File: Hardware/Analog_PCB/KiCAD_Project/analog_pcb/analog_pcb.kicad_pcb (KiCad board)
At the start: 4 copper layers, 44.4 x 31.8 mm, 36 parts, among them J1 Board to Board, U1 555, U2 LF356, U3 LTC1569-6

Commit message: Analog PCB Rev 1.0 complete.
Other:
- board text added: "+5"
- board text added: "-5"
- board text added: "AMP OUT"
- board text added: "ANT"
- board text added: "GND"
- board text added: "NC"

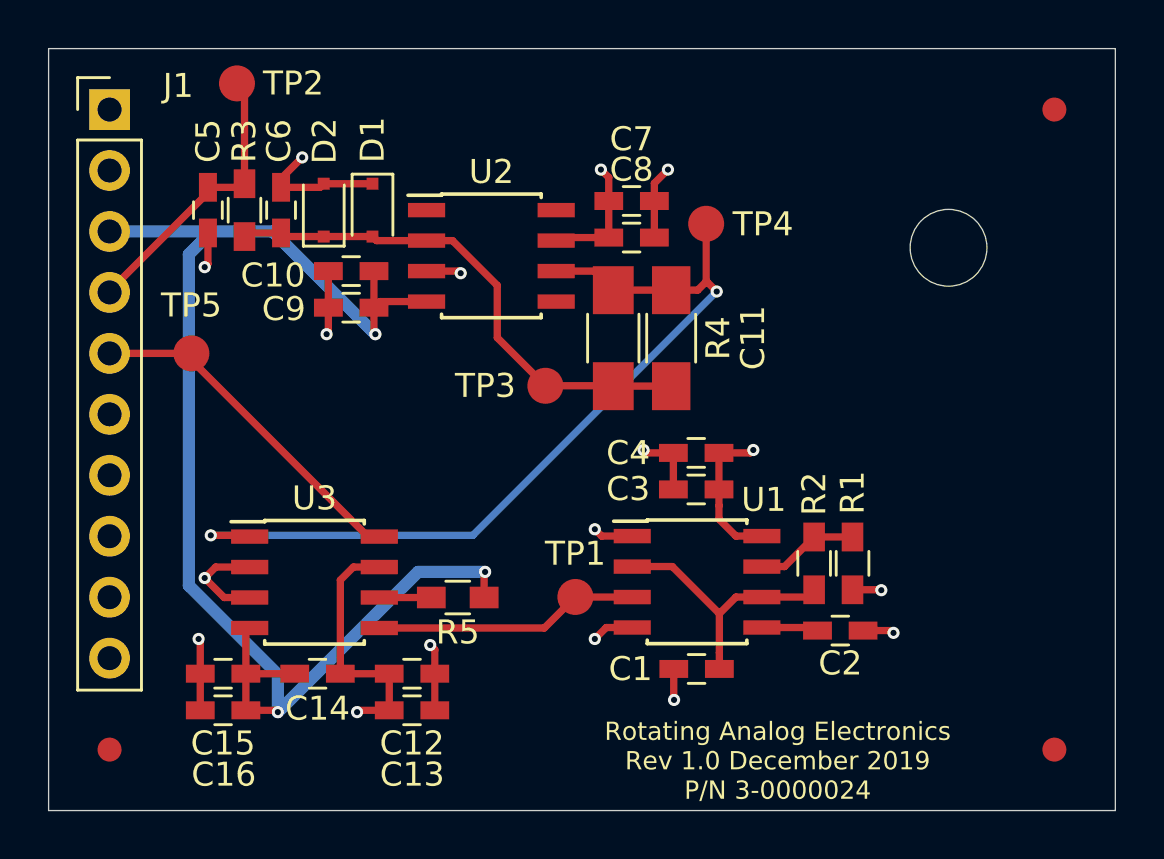
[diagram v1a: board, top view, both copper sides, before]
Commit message: Revise analog PCB for Rev 2.0
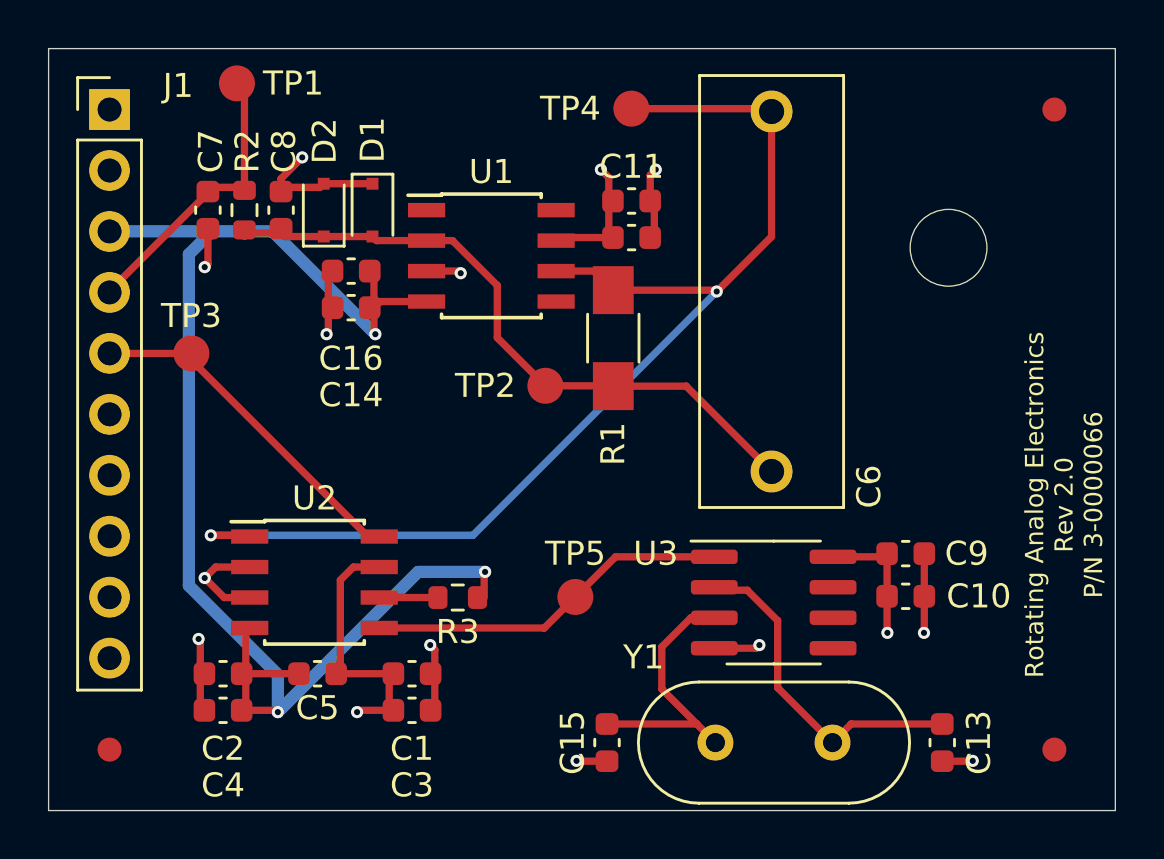
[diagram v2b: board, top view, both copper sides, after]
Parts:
- removed the R1 at (147.9, 85.8)
- removed R5: 10k, Resistors_SMD:R_0603_HandSoldering
- removed the U1 at (141.4, 86.5)
- added U3: ATtiny45-20SU, Package_SO:SOIC-8_3.9x4.9mm_P1.27mm, F.Cu at (144.6, 87.4)
- added Y1: 20MHz, Crystal:Crystal_HC49-U_Vertical, F.Cu at (147.1, 93.2)
- C1, C16, C9: value 0.1u -> 1u; footprint Capacitors_SMD:C_0603_HandSoldering -> Capacitor_SMD:C_0603_1608Metric
- C10, C12, C14, C3: value 1u -> 0.1u; footprint Capacitors_SMD:C_0603_HandSoldering -> Capacitor_SMD:C_0603_1608Metric
- C11: value 0.1u -> 1u; footprint Capacitors_SMD:C_1206_HandSoldering -> Capacitor_SMD:C_0603_1608Metric
- C13: value 0.1u -> 20p; footprint Capacitors_SMD:C_0603_HandSoldering -> Capacitor_SMD:C_0603_1608Metric
- C15: value 1u -> 20p; footprint Capacitors_SMD:C_0603_HandSoldering -> Capacitor_SMD:C_0603_1608Metric
- C2: value 0.01u -> 1u; footprint Capacitors_SMD:C_0603_HandSoldering -> Capacitor_SMD:C_0603_1608Metric
- C4: footprint Capacitors_SMD:C_0603_HandSoldering -> Capacitor_SMD:C_0603_1608Metric
- C5: value 0.39nF -> 1u; footprint Capacitors_SMD:C_0603_HandSoldering -> Capacitor_SMD:C_0603_1608Metric
- C6: value 0.39nF -> 0.1u; footprint Capacitors_SMD:C_0603_HandSoldering -> lib_fp:1-0000787
- C7: value 1u -> 0.39nF; footprint Capacitors_SMD:C_0603_HandSoldering -> Capacitor_SMD:C_0603_1608Metric
- C8: value 0.1u -> 0.39nF; footprint Capacitors_SMD:C_0603_HandSoldering -> Capacitor_SMD:C_0603_1608Metric
- R2: value 4.75k -> 100; footprint Resistors_SMD:R_0603_HandSoldering -> Resistor_SMD:R_0603_1608Metric
- R3: value 100 -> 10k; footprint Resistors_SMD:R_0603_HandSoldering -> Resistor_SMD:R_0603_1608Metric
- moved R2 27.9 mm to (122.6, 71.0), turned to 90 degrees
- moved C10 26.8 mm to (150.1, 87.1), turned to 0 degrees
- moved C2 25.8 mm to (121.7, 90.3), turned to 0 degrees
- moved C9 25.3 mm to (150.1, 85.3), turned to 0 degrees
- moved C4 22.4 mm to (121.7, 91.9), turned to 0 degrees
- moved C13 22.1 mm to (151.6, 93.2), turned to 90 degrees
- moved C6 20.7 mm to (144.5, 74.4), turned to 270 degrees
- moved C12 20.3 mm to (138.7, 72.2)
- moved C5 19.8 mm to (125.6, 90.3), turned to 180 degrees
- moved C16 19.1 mm to (127.0, 73.6), turned to 180 degrees
- moved R3 18.4 mm to (131.4, 87.2), turned to 180 degrees
- moved C7 17.7 mm to (121.0, 71.0), turned to 270 degrees
- moved C15 16.3 mm to (137.7, 93.2), turned to 90 degrees
- moved C14 15.3 mm to (127.0, 75.1)
- moved C3 15.0 mm to (129.5, 91.9), turned to 0 degrees
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- renumbered R4 to R1, TP2 to TP1, TP3 to TP2, TP5 to TP3, TP1 to TP5, U2 to U1, U3 to U2
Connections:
- C1 pad 1: GND -> +5V
- C1 pad 2: Net-(C1-Pad2) -> GND
- C10 pad 1: -5V -> +5V
- C11 pad 1: Net-(C11-Pad1) -> +5V
- C11 pad 2: Net-(C11-Pad2) -> GND
- C13 pad 1: +5V -> GND
- C13 pad 2: GND -> Net-(C13-Pad2)
- C14 pad 1: +5V -> -5V
- C14 pad 2: -5V -> GND
- C15 pad 2: -5V -> Net-(C15-Pad2)
- C16 pad 1: GND -> -5V
- C16 pad 2: -5V -> GND
- C2 pad 2: Net-(C2-Pad2) -> -5V
- C4 pad 1: +5V -> GND
- C4 pad 2: GND -> -5V
- C5 pad 1: In -> +5V
- C5 pad 2: GND -> -5V
- C6 pad 1: Net-(C11-Pad2) -> Net-(C6-Pad1)
- C6 pad 2: GND -> Net-(C6-Pad2)
- C7 pad 1: +5V -> In
- C8 pad 1: +5V -> Net-(C6-Pad2)
- C9 pad 1: -5V -> +5V
- D1 pad 2: Net-(C11-Pad2) -> Net-(C6-Pad2)
- D2 pad 1: Net-(C11-Pad2) -> Net-(C6-Pad2)
- R1 pad 1: Net-(C11-Pad1) -> Net-(C6-Pad1)
- R1 pad 2: Net-(C11-Pad2) -> Net-(C6-Pad2)
- R2 pad 1: Net-(R1-Pad2) -> Net-(C6-Pad2)
- R2 pad 2: Net-(C1-Pad2) -> In
- R3 pad 1: Net-(C11-Pad2) -> -5V
- R3 pad 2: In -> Net-(R3-Pad2)
- TP2 pad 1: Net-(C11-Pad2) -> Net-(C6-Pad2)
- TP4 pad 1: Net-(C11-Pad1) -> Net-(C6-Pad1)
- U1 pad 2: Net-(C11-Pad2) -> Net-(C6-Pad2)
- U1 pad 6: Net-(C11-Pad1) -> Net-(C6-Pad1)
- U2 pad 1: Net-(C11-Pad1) -> Net-(C6-Pad1)
- U2 pad 6: Net-(R5-Pad2) -> Net-(R3-Pad2)
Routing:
- net Net-(C6-Pad1): track 0.00 -> 48.3 mm, vias 0 -> 2
- net Net-(C11-Pad1): track 36.7 -> 0.00 mm, vias 2 -> 0
- net Net-(C6-Pad2): track 0.00 -> 27.4 mm
- net Net-(C11-Pad2): track 21.8 -> 0.00 mm
- net Net-(C13-Pad2): track 0.00 -> 14.1 mm
- net Net-(C15-Pad2): track 0.00 -> 11.3 mm
- net Net-(C1-Pad2): track 11.1 -> 0.00 mm
- net Net-(R1-Pad2): track 4.29 -> 0.00 mm
- net FCLK: track 11.1 -> 15.2 mm
- net +5V: track 25.2 -> 21.5 mm, vias 5 -> 3
- net Net-(C2-Pad2): track 2.37 -> 0.00 mm
- net Net-(R5-Pad2): track 2.17 -> 0.00 mm
- net Net-(R3-Pad2): track 0.00 -> 2.17 mm
- net GND: track 31.3 -> 31.9 mm
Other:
- rule pad_to_mask_clearance: 0.051 -> 0
- board text added: "Rotating Analog Electronics Rev 2.0 P/N 3-0000066"
- board text removed: "Rotating Analog Electronics Rev 1.0 December 2019 P/N 3-0000024"

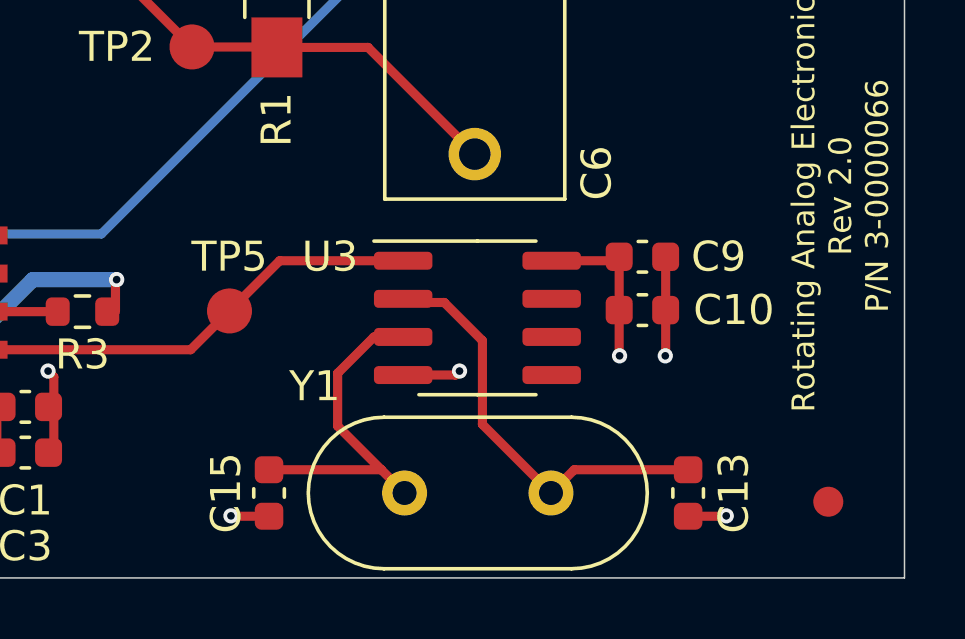
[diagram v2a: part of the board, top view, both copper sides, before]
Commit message: Fix footprint for ATTINY
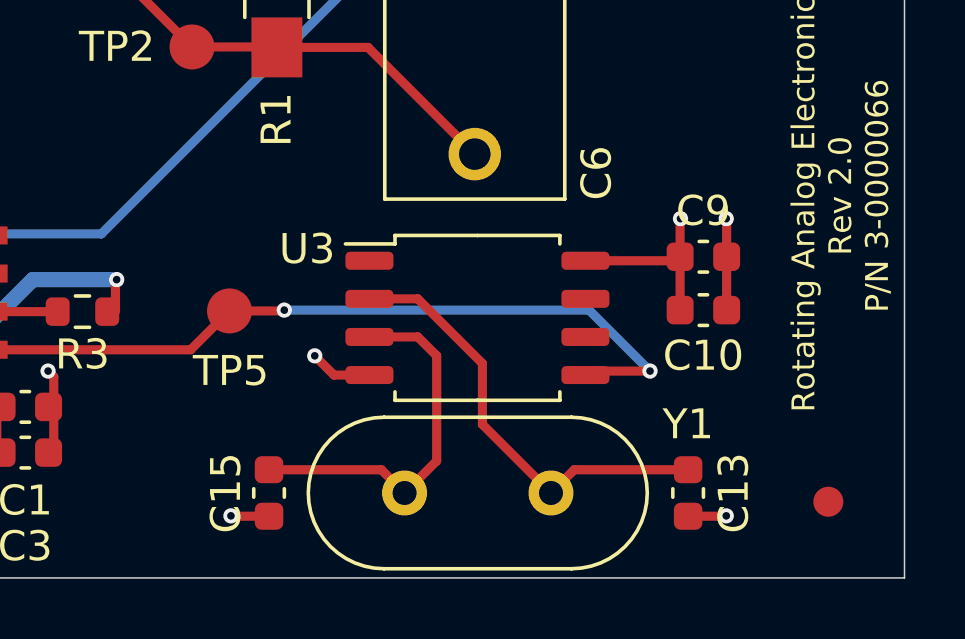
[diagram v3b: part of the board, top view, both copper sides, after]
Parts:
- added PCB1: barepcb, misc:barepcb, F.Cu at (275.3, 20.3)
- U3: footprint Package_SO:SOIC-8_3.9x4.9mm_P1.27mm -> Package_SO:SOIC-8_5.275x5.275mm_P1.27mm
- moved C10 2.03 mm to (152.1, 87.1)
- moved C9 2.03 mm to (152.1, 85.3)
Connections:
- U3 pad 1: FCLK -> (no net)
- U3 pad 5: (no net) -> FCLK
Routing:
- net FCLK: track 15.2 -> 25.8 mm, vias 0 -> 2
- net Net-(C15-Pad2): track 11.3 -> 12.4 mm
- net Net-(C13-Pad2): track 14.1 -> 14.8 mm
- net +5V: track 21.5 -> 22.2 mm

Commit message: Add Analog PCB REV 2.1 files
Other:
- board text added: "Rotating Analog Electronics Rev 2.1 3-0000081/7-0000037"
- board text removed: "Rotating Analog Electronics Rev 2.0 P/N 3-0000066"
